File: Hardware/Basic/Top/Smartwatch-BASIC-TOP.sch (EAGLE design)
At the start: 52 parts, among them U2 NRF52832_MODULE_MDBT42, U4 CP2104

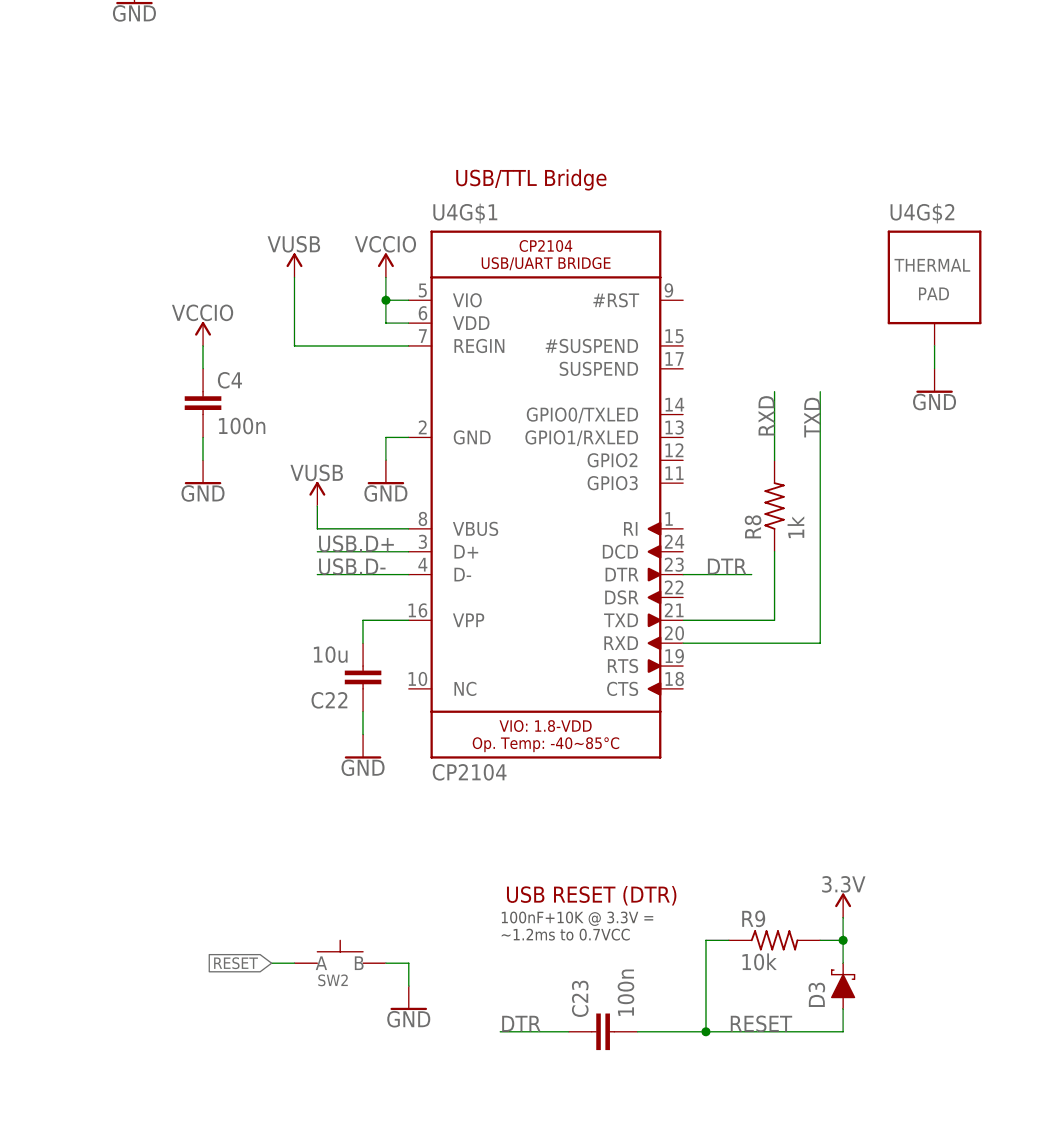
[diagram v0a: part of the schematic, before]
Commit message: USB, OLED Microcontroller and SD added. Need to add RTC
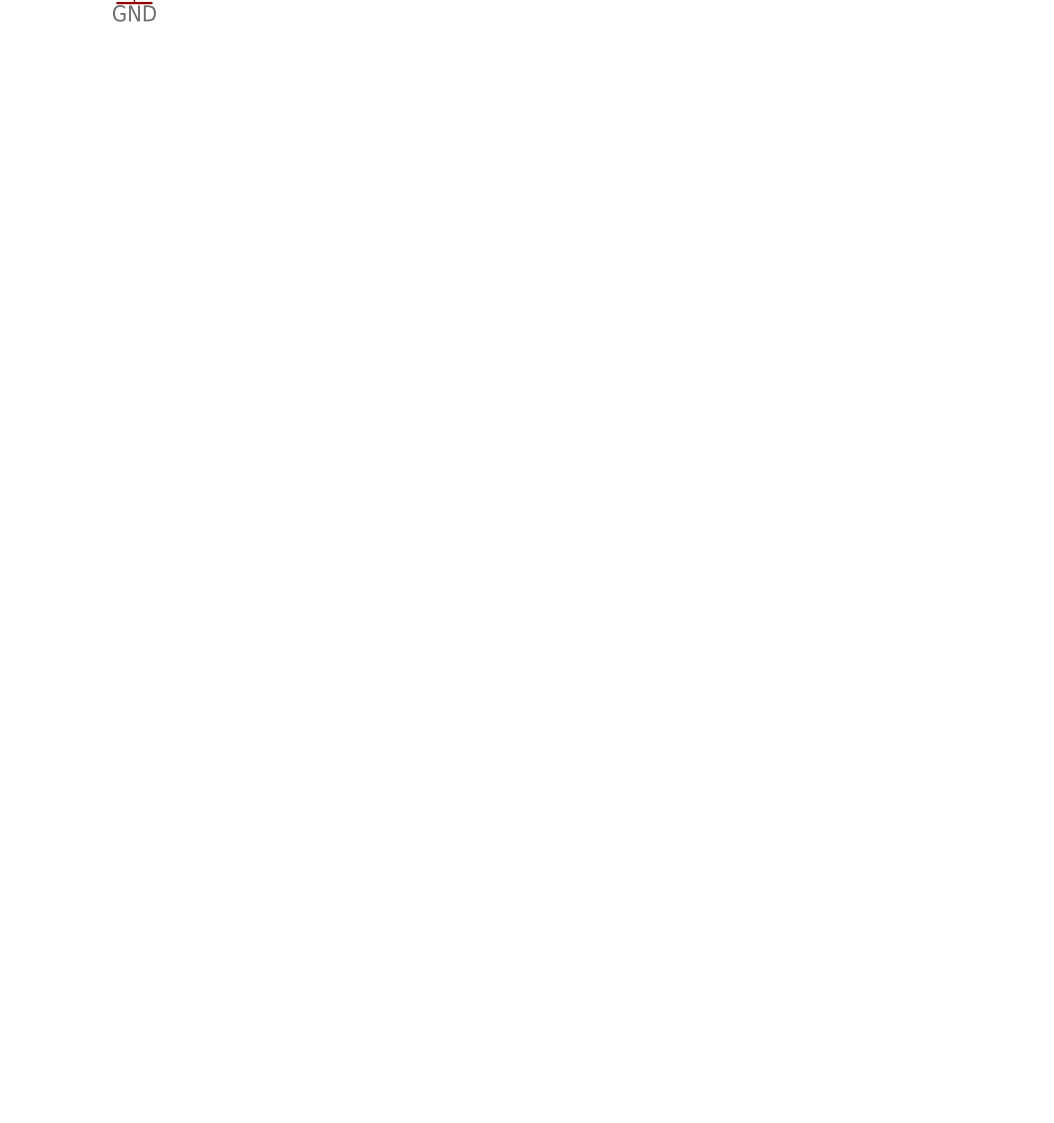
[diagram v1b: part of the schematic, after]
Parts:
- removed C22: 10u, LinnesLab-Passives:CAPACITOR0805
- removed C23, C4: 100n, LinnesLab-Passives:CAPACITOR0603
- removed D3: (no value), LinnesLab-DiscreteSemi:SCHOTTKY-USC
- removed R8: 1k, LinnesLab-Passives:RESISTOR0603
- removed R9: 10k, LinnesLab-Passives:RESISTOR0603
- removed SW2: (no value), LinnesLab-Switches:SPST-PTS830GG140-COPY.1-3
- removed U4: CP2104, LinnesLab-DigitalIC:CP2104
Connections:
- removed net N$19: R8.1, U4G$1.TXD
- removed net N$20: C22.2, U4G$1.VPP
- removed net USB.D+: U4G$1.D+
- removed net USB.D-: U4G$1.D-
- removed net VCCIO: C4.1, U4G$1.VDD, U4G$1.VIO
- net 3.3V: no longer D3.C, R9.2
- net DTR: no longer C23.1, U4G$1.DTR
- net GND: no longer C22.1, C4.2, SW2.B, U4G$1.GND, U4G$2.TP
- net N$1: no longer U4G$1.VBUS
- net RESET: no longer C23.2, D3.A, R9.1, SW2.A
- net RXD: no longer R8.2
- net TXD: no longer U4G$1.RXD
- net V_USB: no longer U4G$1.REGIN
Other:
- note removed: "USB RESET (DTR)"
- note removed: "USB/TTL Bridge"

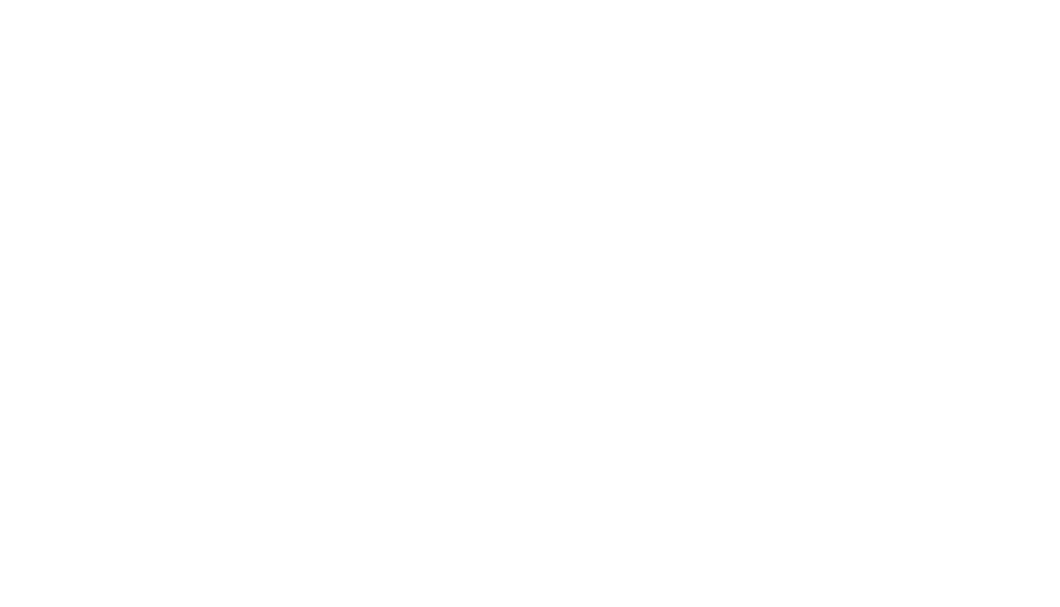
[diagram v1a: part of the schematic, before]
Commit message: USB, OLED Microcontroller, SD and RTC added
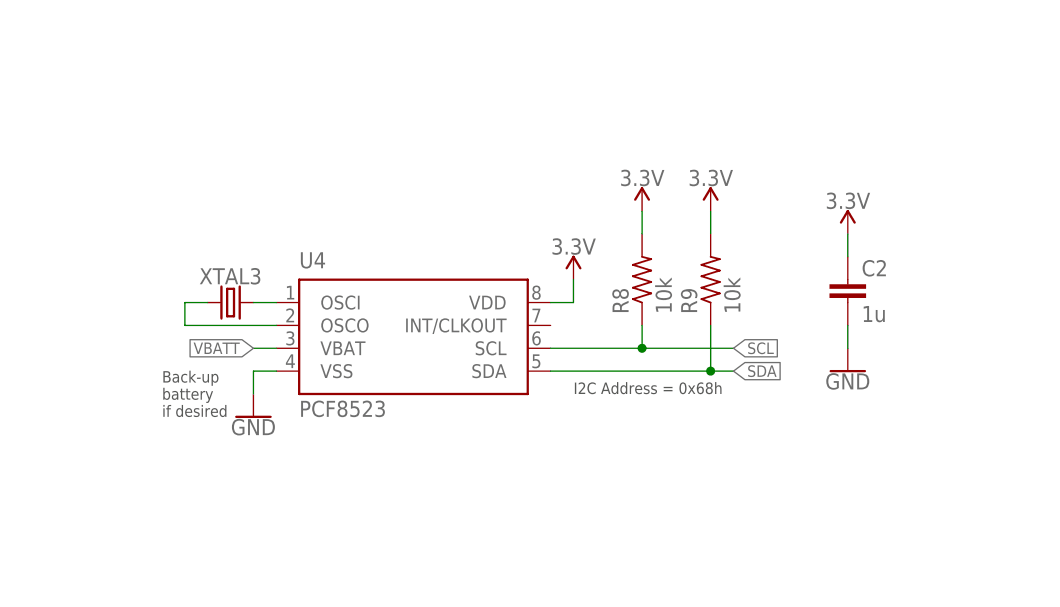
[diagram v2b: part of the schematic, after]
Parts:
- added C2: 1u, LinnesLab-Passives:CAPACITOR0603
- added R8, R9: 10k, LinnesLab-Passives:RESISTOR0603
- added U4: PCF8523, LinnesLab-Clocks:PCF8523
- added XTAL3: 32.7680kHz, LinnesLab-Clocks:CRYSTALECS-.327-12.5-12-C-TR
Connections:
- new net N$19: U4.OSCO, XTAL3.1
- new net N$20: U4.OSCI, XTAL3.2
- new net VBATT: U4.VBAT
- net 3.3V: now also C2.1, R8.2, R9.2, U4.VDD
- net GND: now also C2.2, U4.VSS
- net SCL: now also R8.1, U4.SCL
- net SDA: now also R9.1, U4.SDA
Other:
- note added: "Back-up battery if desired"
- note added: "I2C Address = 0x68h"
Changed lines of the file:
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@@
 <part name="GND2" library="LinnesLab-Symbols" deviceset="GND" device=""/>
 <part name="SD2" library="LinnesLab-Connectors" deviceset="MICROSD" device="" package3d_urn="urn:adsk.eagle:package:17873109/2"/>
+<part name="GND4" library="LinnesLab-Symbols" deviceset="GND" device=""/>
+<part name="GND5" library="LinnesLab-Symbols" deviceset="GND" device=""/>
+<part name="SUPPLY10" library="LinnesLab-Symbols" deviceset="3.3V" device=""/>
+<part name="C2" library="LinnesLab-Passives" deviceset="CAPACITOR" device="0603" package3d_urn="urn:adsk.eagle:package:15661989/2" value="1u"/>
+<part name="SUPPLY17" library="LinnesLab-Symbols" deviceset="3.3V" device=""/>
+<part name="R8" library="LinnesLab-Passives" deviceset="RESISTOR" device="0603" package3d_urn="urn:adsk.eagle:package:15661944/2" value="10k"/>
+<part name="R9" library="LinnesLab-Passives" deviceset="RESISTOR" device="0603" package3d_urn="urn:adsk.eagle:package:15661944/2" value="10k"/>
+<part name="SUPPLY18" library="LinnesLab-Symbols" deviceset="3.3V" device=""/>
+<part name="SUPPLY19" library="LinnesLab-Symbols" deviceset="3.3V" device=""/>
+<part name="XTAL3" library="LinnesLab-Clocks" deviceset="CRYSTAL" device="ECS-.327-12.5-12-C-TR" package3d_urn="urn:adsk.eagle:package:18579459/2" value="32.7680kHz">
+<attribute name="FREQ" value="32.7680KHZ"/>
+</part>
+<part name="U4" library="LinnesLab-Clocks" deviceset="PCF8523" device="" package3d_urn="urn:adsk.eagle:package:18599600/2">
+<attribute name="DIGIKEY" value="568-5306-1-ND"/>
+<attribute name="I2C_ADDRESS" value="0x68h"/>
+<attribute name="MFN" value="PCF8523T/1,118"/>
+<attribute name="MFN_MANUFACTURER" value="NXP USA Inc."/>
+</part>
 </parts>
 <sheets>
@@
 You have more flexibility with the
 SD.CS pin.</text>
+<text x="292.1" y="-22.86" size="1.27" layer="97">I2C Address = 0x68h</text>
+<text x="246.38" y="-25.4" size="1.27" layer="97">Back-up
+battery
+if desired</text>
 </plain>
 <instances>
@@
 <attribute name="NAME" x="327.66" y="130.81" size="1.778" layer="95"/>
 <attribute name="VALUE" x="345.44" y="130.81" size="1.778" layer="96"/>
+</instance>
+<instance part="GND4" gate="G$1" x="256.54" y="-25.4" smashed="yes">
+<attribute name="VALUE" x="256.54" y="-25.654" size="1.778" layer="96" align="top-center"/>
+</instance>
+<instance part="GND5" gate="G$1" x="322.58" y="-20.32" smashed="yes">
+<attribute name="VALUE" x="322.58" y="-20.574" size="1.778" layer="96" align="top-center"/>
+</instance>
+<instance part="SUPPLY10" gate="G$1" x="292.1" y="-10.16" smashed="yes">
+<attribute name="VALUE" x="292.1" y="-7.366" size="1.778" layer="96" align="bottom-center"/>
+</instance>
+<instance part="C2" gate="G$1" x="322.58" y="-12.7" smashed="yes">
+<attribute name="NAME" x="324.104" y="-9.779" size="1.778" layer="95"/>
+<attribute name="VALUE" x="324.104" y="-14.859" size="1.778" layer="96"/>
+</instance>
+<instance part="SUPPLY17" gate="G$1" x="322.58" y="-5.08" smashed="yes">
+<attribute name="VALUE" x="322.58" y="-2.286" size="1.778" layer="96" align="bottom-center"/>
+</instance>
+<instance part="R8" gate="G$1" x="299.72" y="-10.16" smashed="yes" rot="R90">
+<attribute name="NAME" x="298.2214" y="-13.97" size="1.778" layer="95" rot="R90"/>
+<attribute name="VALUE" x="303.022" y="-13.97" size="1.778" layer="96" rot="R90"/>
+</instance>
+<instance part="R9" gate="G$1" x="307.34" y="-10.16" smashed="yes" rot="R90">
+<attribute name="NAME" x="305.8414" y="-13.97" size="1.778" layer="95" rot="R90"/>
+<attribute name="VALUE" x="310.642" y="-13.97" size="1.778" layer="96" rot="R90"/>
+</instance>
+<instance part="SUPPLY18" gate="G$1" x="299.72" y="-2.54" smashed="yes">
+<attribute name="VALUE" x="299.72" y="0.254" size="1.778" layer="96" align="bottom-center"/>
+</instance>
+<instance part="SUPPLY19" gate="G$1" x="307.34" y="-2.54" smashed="yes">
+<attribute name="VALUE" x="307.34" y="0.254" size="1.778" layer="96" align="bottom-center"/>
+</instance>
+<instance part="XTAL3" gate="G$1" x="254" y="-12.7" smashed="yes">
+<attribute name="NAME" x="254" y="-10.668" size="1.778" layer="95" font="vector" align="bottom-center"/>
+<attribute name="FREQ" x="254" y="-12.7" size="1.27" layer="96" display="off"/>
+</instance>
+<instance part="U4" gate="G$1" x="274.32" y="-15.24" smashed="yes">
+<attribute name="NAME" x="261.62" y="-8.89" size="1.778" layer="95"/>
+<attribute name="VALUE" x="261.62" y="-25.4" size="1.778" layer="96"/>
+<attribute name="DIGIKEY" x="274.32" y="-15.24" size="1.27" layer="96" display="off"/>
+<attribute name="I2C_ADDRESS" x="274.32" y="-15.24" size="1.27" layer="96" display="off"/>
+<attribute name="MFN" x="274.32" y="-15.24" size="1.27" layer="96" display="off"/>
+<attribute name="MFN_MANUFACTURER" x="274.32" y="-15.24" size="1.27" layer="96" display="off"/>
 </instance>
 </instances>
@@
 <pinref part="SD2" gate="G$1" pin="GND1"/>
 </segment>
+<segment>
+<wire x1="259.08" y1="-20.32" x2="256.54" y2="-20.32" width="0.1524" layer="91"/>
+<wire x1="256.54" y1="-22.86" x2="256.54" y2="-20.32" width="0.1524" layer="91"/>
+<pinref part="GND4" gate="G$1" pin="GND"/>
+<pinref part="U4" gate="G$1" pin="VSS"/>
+</segment>
+<segment>
+<wire x1="322.58" y1="-17.78" x2="322.58" y2="-15.24" width="0.1524" layer="91"/>
+<pinref part="GND5" gate="G$1" pin="GND"/>
+<pinref part="C2" gate="G$1" pin="2"/>
+</segment>
 </net>
 <net name="SWDIO" class="0">
@@
 <pinref part="SD2" gate="G$1" pin="VDD"/>
 </segment>
+<segment>
+<wire x1="289.56" y1="-12.7" x2="292.1" y2="-12.7" width="0.1524" layer="91"/>
+<wire x1="292.1" y1="-10.16" x2="292.1" y2="-12.7" width="0.1524" layer="91"/>
+<pinref part="SUPPLY10" gate="G$1" pin="3.3V"/>
+<pinref part="U4" gate="G$1" pin="VDD"/>
+</segment>
+<segment>
+<pinref part="C2" gate="G$1" pin="1"/>
+<pinref part="SUPPLY17" gate="G$1" pin="3.3V"/>
+<wire x1="322.58" y1="-5.08" x2="322.58" y2="-7.62" width="0.1524" layer="91"/>
+</segment>
+<segment>
+<pinref part="R8" gate="G$1" pin="2"/>
+<pinref part="SUPPLY18" gate="G$1" pin="3.3V"/>
+<wire x1="299.72" y1="-2.54" x2="299.72" y2="-5.08" width="0.1524" layer="91"/>
+</segment>
+<segment>
+<pinref part="R9" gate="G$1" pin="2"/>
+<pinref part="SUPPLY19" gate="G$1" pin="3.3V"/>
+<wire x1="307.34" y1="-2.54" x2="307.34" y2="-5.08" width="0.1524" layer="91"/>
+</segment>
 </net>
 <net name="SDA" class="0">
@@
 <pinref part="U2" gate="G$1" pin="P0.25"/>
 </segment>
+<segment>
+<wire x1="289.56" y1="-20.32" x2="307.34" y2="-20.32" width="0.1524" layer="91"/>
+<label x="309.88" y="-20.32" size="1.27" layer="95" xref="yes"/>
+<pinref part="R9" gate="G$1" pin="1"/>
+<wire x1="307.34" y1="-20.32" x2="309.88" y2="-20.32" width="0.1524" layer="91"/>
+<wire x1="307.34" y1="-15.24" x2="307.34" y2="-20.32" width="0.1524" layer="91"/>
+<junction x="307.34" y="-20.32"/>
+<pinref part="U4" gate="G$1" pin="SDA"/>
+</segment>
 </net>
 <net name="SCL" class="0">
@@
 <label x="63.5" y="104.14" size="1.27" layer="95" rot="R180" xref="yes"/>
 <pinref part="U2" gate="G$1" pin="P0.26"/>
+</segment>
+<segment>
+<wire x1="289.56" y1="-17.78" x2="299.72" y2="-17.78" width="0.1524" layer="91"/>
+<label x="309.88" y="-17.78" size="1.27" layer="95" xref="yes"/>
+<pinref part="R8" gate="G$1" pin="1"/>
+<wire x1="299.72" y1="-17.78" x2="309.88" y2="-17.78" width="0.1524" layer="91"/>
+<wire x1="299.72" y1="-15.24" x2="299.72" y2="-17.78" width="0.1524" layer="91"/>
+<junction x="299.72" y="-17.78"/>
+<pinref part="U4" gate="G$1" pin="SCL"/>
 </segment>
 </net>
@@
 </segment>
 </net>
+<net name="N$19" class="0">
+<segment>
+<wire x1="259.08" y1="-15.24" x2="248.92" y2="-15.24" width="0.1524" layer="91"/>
+<wire x1="248.92" y1="-15.24" x2="248.92" y2="-12.7" width="0.1524" layer="91"/>
+<wire x1="248.92" y1="-12.7" x2="251.46" y2="-12.7" width="0.1524" layer="91"/>
+<pinref part="XTAL3" gate="G$1" pin="1"/>
+<pinref part="U4" gate="G$1" pin="OSCO"/>
+</segment>
+</net>
+<net name="N$20" class="0">
+<segment>
+<wire x1="256.54" y1="-12.7" x2="259.08" y2="-12.7" width="0.1524" layer="91"/>
+<pinref part="XTAL3" gate="G$1" pin="2"/>
+<pinref part="U4" gate="G$1" pin="OSCI"/>
+</segment>
+</net>
+<net name="VBATT" class="0">
+<segment>
+<wire x1="259.08" y1="-17.78" x2="256.54" y2="-17.78" width="0.1524" layer="91"/>
+<label x="256.54" y="-17.78" size="1.27" layer="95" rot="R180" xref="yes"/>
+<pinref part="U4" gate="G$1" pin="VBAT"/>
+</segment>
+</net>

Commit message: Added FTDI
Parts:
- removed C2: 1u, LinnesLab-Passives:CAPACITOR0603
- removed R8, R9: 10k, LinnesLab-Passives:RESISTOR0603
- removed XTAL3: 32.7680kHz, LinnesLab-Clocks:CRYSTALECS-.327-12.5-12-C-TR
- added C22, C23: 47p, LinnesLab-Passives:CAPACITOR0603
- added C4: 100n, LinnesLab-Passives:CAPACITOR0603
- added J1: (no value), LinnesLab-Connectors:CONN_07
- added JP2: (no value), LinnesLab-Switches:JUMPER-SMT_2_NO_SILK
- added LED5: RED, LinnesLab-LED:LED0603
- added LED6: YELLOW, LinnesLab-LED:LED0603
- added R1, R2: 10k, LinnesLab-Passives:RESISTOR0603
- added R10, R16: 27, LinnesLab-Passives:RESISTOR0603
- added R17, R18: 1k, LinnesLab-Passives:RESISTOR0603
- added SW6, SW7: SWITCH.MOM, LinnesLab-Switches:SWITCH.MOM
- U4: value PCF8523 -> FT231XS; device LinnesLab-Clocks:PCF8523 -> LinnesLab-DigitalIC:FT231XS; DIGIKEY 568-5306-1-ND -> (none); I2C_ADDRESS 0x68h -> (none); MFN PCF8523T/1,118 -> (none); MFN_MANUFACTURER NXP USA Inc. -> (none)
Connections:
- removed net BATT: R13.1, R14.2
- removed net CD1: SD2.CARD_DETECT
- removed net CHRG.STAT: CHRG2.STAT, R12.1
- removed net N$19: U4.OSCO, XTAL3.1
- removed net N$20: U4.OSCI, XTAL3.2
- removed net SD.CS: SD2.CS
- removed net VBATT: U4.VBAT
- new net !CTS: JP2.2, U4.!CTS
- new net !DTR: U4.!DTR
- new net A4/BATT: R13.1, R14.2, U2.P0.28/AIN4
- new net D27/CHRG.STAT: CHRG2.STAT, R12.1, U2.P0.27
- new net D5/CD1: SD2.CARD_DETECT, U2.P0.05/AIN3
- new net D7/SD.CS: SD2.CS, U2.P0.07
- new net FT3V3: U4.3V3OUT
- new net N$21: SW7.3, SW7.4
- new net N$22: SW6.3, SW6.4
- new net N$23: SW6.1
- new net N$24: SW7.1
- new net N$25: R10.2, U4.USBDM
- new net N$26: R16.2, U4.USBDP
- new net N$27: LED5.C, R17.2
- new net N$28: LED6.C, R18.2
- new net RXLED: R17.1, U4.CBUS1
- new net TXLED: R18.1, U4.CBUS2
- net 3.3V: now also C4.2, LED5.A, LED6.A, R1.2, R2.2, U4.!RESET, U4.VCCIO; no longer C2.1, R8.2, R9.2, U4.VDD
- net GND: now also C22.2, C23.1, C4.1, JP2.1, U4.GND@16, U4.GND@6; no longer C2.2, U4.VSS
- net RXD: now also U4.RXD
- net SCL: now also R2.1; no longer R8.1, U4.SCL
- net SDA: now also R1.1; no longer R9.1, U4.SDA
- net TXD: now also U4.TXD
- net USB+: now also C22.1, R16.1
- net USB-: now also C23.2, R10.1
- net V_USB: now also U4.VCC
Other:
- note added: "I don't remember if CTS needs to be grounded or left floating so here's a jumper to ground so it can be configued either way dynamically."
- note added: "TXD goes to RX on the other device RXD goes to TX on the other device"
- note removed: "Back-up battery if desired"
- note removed: "I2C Address = 0x68h"
- moved on the sheet: SD2
